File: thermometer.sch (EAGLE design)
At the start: 36 parts, among them IC1 MAX232, Q2 4 MHz, T1 BC547, T2 BC547, T3 BC547, T6 BC547, T7 BC547, T8 BC547, T9 BC547, X2 MINI-USB_SHIELD4P-85-32004-10X

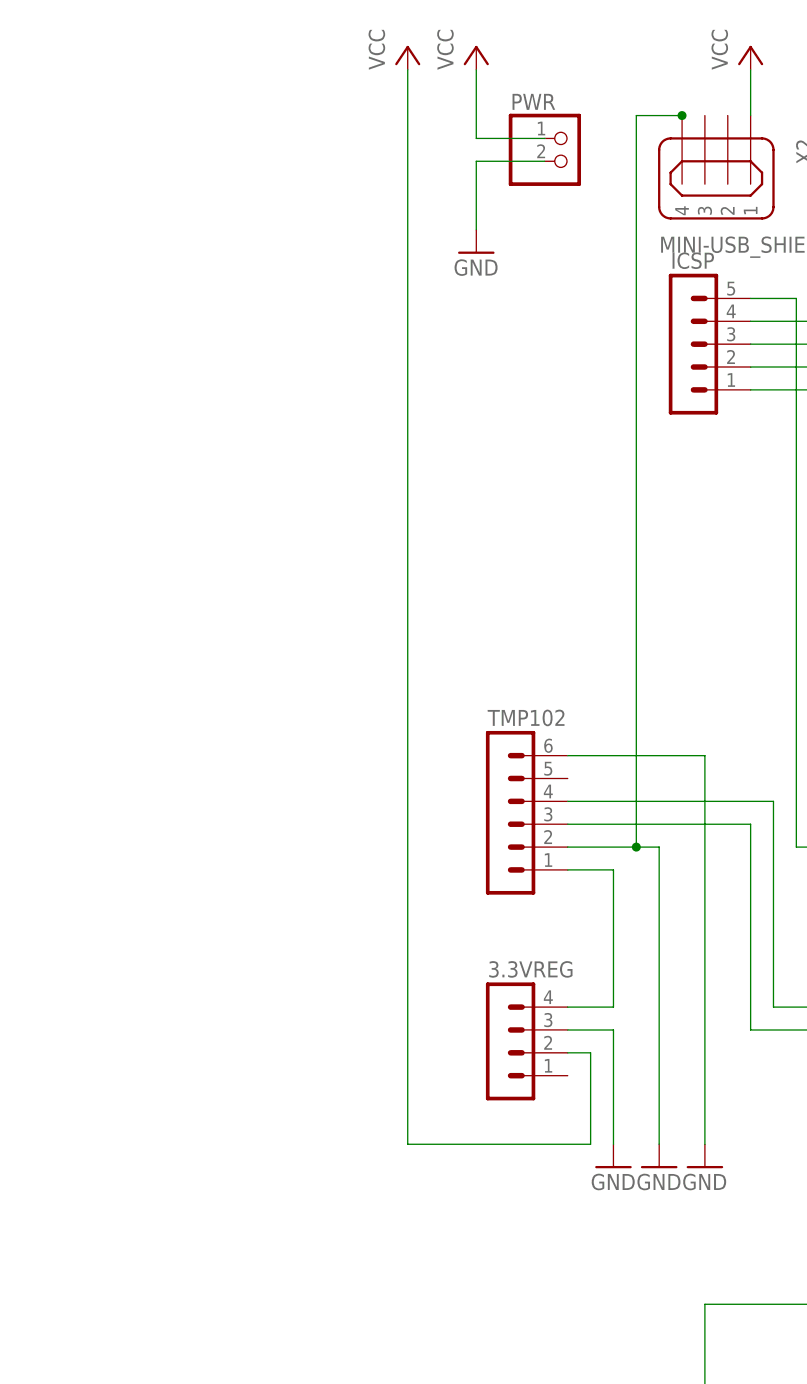
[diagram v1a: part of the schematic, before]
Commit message: Adding schematic and board as images
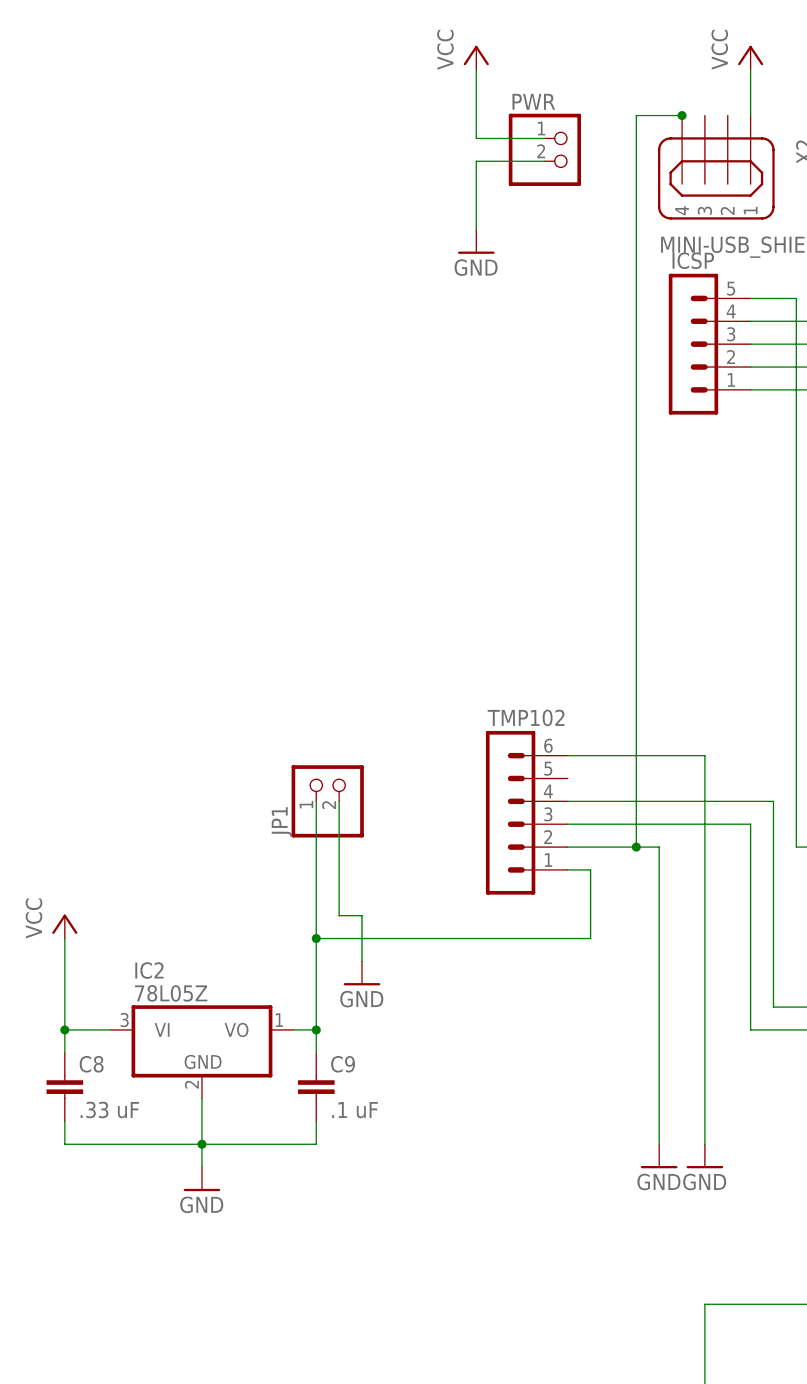
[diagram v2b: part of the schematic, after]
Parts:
- removed 3.3VREG: (no value), con-lstb:MA04-1
- added C8: .33 uF, rcl:C-EU050-025X075
- added C9: .1 uF, rcl:C-EU050-025X075
- added IC2: 78L05Z, linear:78L05Z
- added JP1: (no value), pinhead:PINHD-1X2
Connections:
- removed net N$32: 3.3VREG.4, TMP102.1
- new net N$48: C9.1, IC2.VO, JP1.1, TMP102.1
- net GND: now also C8.2, C9.2, IC2.GND, JP1.2; no longer 3.3VREG.3
- net VCC: now also C8.1, IC2.VI; no longer 3.3VREG.2
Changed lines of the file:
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@@
 <part name="ICSP" library="con-lstb" deviceset="MA05-1" device=""/>
 <part name="TMP102" library="con-lstb" deviceset="MA06-1" device=""/>
-<part name="3.3VREG" library="con-lstb" deviceset="MA04-1" device=""/>
-<part name="P+5" library="supply1" deviceset="VCC" device=""/>
-<part name="GND14" library="supply1" deviceset="GND" device=""/>
 <part name="GND15" library="supply1" deviceset="GND" device=""/>
 <part name="GND16" library="supply1" deviceset="GND" device=""/>
@@
 <part name="X2" library="con-cypressindustries" deviceset="MINI-USB_SHIELD4P-" device="85-32004-10X"/>
 <part name="P+8" library="supply1" deviceset="VCC" device=""/>
+<part name="IC2" library="linear" deviceset="78*" device="Z" technology="L05"/>
+<part name="C8" library="rcl" deviceset="C-EU" device="050-025X075" value=".33 uF"/>
+<part name="C9" library="rcl" deviceset="C-EU" device="050-025X075" value=".1 uF"/>
+<part name="GND20" library="supply1" deviceset="GND" device=""/>
+<part name="P+9" library="supply1" deviceset="VCC" device=""/>
+<part name="JP1" library="pinhead" deviceset="PINHD-1X2" device=""/>
+<part name="GND21" library="supply1" deviceset="GND" device=""/>
 </parts>
 <sheets>
@@
 <instance part="ICSP" gate="G$1" x="-55.88" y="210.82"/>
 <instance part="TMP102" gate="1" x="-76.2" y="160.02"/>
-<instance part="3.3VREG" gate="1" x="-76.2" y="134.62"/>
-<instance part="P+5" gate="VCC" x="-86.36" y="243.84"/>
-<instance part="GND14" gate="1" x="-63.5" y="119.38"/>
 <instance part="GND15" gate="1" x="-58.42" y="119.38"/>
 <instance part="GND16" gate="1" x="-53.34" y="119.38"/>
@@
 <instance part="X2" gate="G$1" x="-53.34" y="231.14" rot="R270"/>
 <instance part="P+8" gate="VCC" x="-48.26" y="243.84"/>
+<instance part="IC2" gate="A1" x="-109.22" y="134.62"/>
+<instance part="C8" gate="G$1" x="-124.46" y="129.54"/>
+<instance part="C9" gate="G$1" x="-96.52" y="129.54"/>
+<instance part="GND20" gate="1" x="-109.22" y="116.84"/>
+<instance part="P+9" gate="VCC" x="-124.46" y="147.32"/>
+<instance part="JP1" gate="G$1" x="-93.98" y="162.56" rot="R90"/>
+<instance part="GND21" gate="1" x="-91.44" y="139.7"/>
 </instances>
 <busses>
@@
 <wire x1="-48.26" y1="210.82" x2="-35.56" y2="210.82" width="0.1524" layer="91"/>
 <wire x1="-35.56" y1="210.82" x2="-35.56" y2="185.42" width="0.1524" layer="91"/>
-</segment>
-<segment>
-<pinref part="3.3VREG" gate="1" pin="3"/>
-<pinref part="GND14" gate="1" pin="GND"/>
-<wire x1="-68.58" y1="134.62" x2="-63.5" y2="134.62" width="0.1524" layer="91"/>
-<wire x1="-63.5" y1="134.62" x2="-63.5" y2="121.92" width="0.1524" layer="91"/>
 </segment>
 <segment>
@@
 <wire x1="-71.12" y1="231.14" x2="-78.74" y2="231.14" width="0.1524" layer="91"/>
 <wire x1="-78.74" y1="231.14" x2="-78.74" y2="223.52" width="0.1524" layer="91"/>
+</segment>
+<segment>
+<pinref part="IC2" gate="A1" pin="GND"/>
+<pinref part="GND20" gate="1" pin="GND"/>
+<wire x1="-109.22" y1="127" x2="-109.22" y2="121.92" width="0.1524" layer="91"/>
+<pinref part="C8" gate="G$1" pin="2"/>
+<wire x1="-109.22" y1="121.92" x2="-109.22" y2="119.38" width="0.1524" layer="91"/>
+<wire x1="-124.46" y1="124.46" x2="-124.46" y2="121.92" width="0.1524" layer="91"/>
+<wire x1="-124.46" y1="121.92" x2="-109.22" y2="121.92" width="0.1524" layer="91"/>
+<pinref part="C9" gate="G$1" pin="2"/>
+<wire x1="-96.52" y1="124.46" x2="-96.52" y2="121.92" width="0.1524" layer="91"/>
+<wire x1="-96.52" y1="121.92" x2="-109.22" y2="121.92" width="0.1524" layer="91"/>
+<junction x="-109.22" y="121.92"/>
+</segment>
+<segment>
+<pinref part="JP1" gate="G$1" pin="2"/>
+<wire x1="-93.98" y1="160.02" x2="-93.98" y2="147.32" width="0.1524" layer="91"/>
+<pinref part="GND21" gate="1" pin="GND"/>
+<wire x1="-93.98" y1="147.32" x2="-91.44" y2="147.32" width="0.1524" layer="91"/>
+<wire x1="-91.44" y1="147.32" x2="-91.44" y2="142.24" width="0.1524" layer="91"/>
 </segment>
 </net>
@@
 </segment>
 <segment>
-<pinref part="P+5" gate="VCC" pin="VCC"/>
-<wire x1="-86.36" y1="241.3" x2="-86.36" y2="121.92" width="0.1524" layer="91"/>
-<wire x1="-86.36" y1="121.92" x2="-66.04" y2="121.92" width="0.1524" layer="91"/>
-<wire x1="-66.04" y1="121.92" x2="-66.04" y2="132.08" width="0.1524" layer="91"/>
-<pinref part="3.3VREG" gate="1" pin="2"/>
-<wire x1="-66.04" y1="132.08" x2="-68.58" y2="132.08" width="0.1524" layer="91"/>
-</segment>
-<segment>
 <pinref part="C6" gate="G$1" pin="-"/>
 <pinref part="P+6" gate="VCC" pin="VCC"/>
@@
 <pinref part="X2" gate="G$1" pin="1"/>
 <wire x1="-48.26" y1="241.3" x2="-48.26" y2="236.22" width="0.1524" layer="91"/>
+</segment>
+<segment>
+<pinref part="IC2" gate="A1" pin="VI"/>
+<pinref part="C8" gate="G$1" pin="1"/>
+<wire x1="-119.38" y1="134.62" x2="-124.46" y2="134.62" width="0.1524" layer="91"/>
+<wire x1="-124.46" y1="134.62" x2="-124.46" y2="132.08" width="0.1524" layer="91"/>
+<pinref part="P+9" gate="VCC" pin="VCC"/>
+<wire x1="-124.46" y1="144.78" x2="-124.46" y2="134.62" width="0.1524" layer="91"/>
+<junction x="-124.46" y="134.62"/>
 </segment>
 </net>
@@
 <pinref part="PIC16F877A" gate="A" pin="RB7/PGD"/>
 <wire x1="-40.64" y1="157.48" x2="30.48" y2="157.48" width="0.1524" layer="91"/>
-</segment>
-</net>
-<net name="N$32" class="0">
-<segment>
-<pinref part="TMP102" gate="1" pin="1"/>
-<wire x1="-68.58" y1="152.4" x2="-63.5" y2="152.4" width="0.1524" layer="91"/>
-<wire x1="-63.5" y1="152.4" x2="-63.5" y2="137.16" width="0.1524" layer="91"/>
-<pinref part="3.3VREG" gate="1" pin="4"/>
-<wire x1="-63.5" y1="137.16" x2="-68.58" y2="137.16" width="0.1524" layer="91"/>
 </segment>
 </net>
@@
 </segment>
 </net>
+<net name="N$48" class="0">
+<segment>
+<pinref part="IC2" gate="A1" pin="VO"/>
+<pinref part="C9" gate="G$1" pin="1"/>
+<wire x1="-99.06" y1="134.62" x2="-96.52" y2="134.62" width="0.1524" layer="91"/>
+<wire x1="-96.52" y1="134.62" x2="-96.52" y2="132.08" width="0.1524" layer="91"/>
+<pinref part="JP1" gate="G$1" pin="1"/>
+<wire x1="-96.52" y1="134.62" x2="-96.52" y2="144.78" width="0.1524" layer="91"/>
+<junction x="-96.52" y="134.62"/>
+<pinref part="TMP102" gate="1" pin="1"/>
+<wire x1="-96.52" y1="144.78" x2="-96.52" y2="160.02" width="0.1524" layer="91"/>
+<wire x1="-68.58" y1="152.4" x2="-66.04" y2="152.4" width="0.1524" layer="91"/>
+<wire x1="-66.04" y1="152.4" x2="-66.04" y2="144.78" width="0.1524" layer="91"/>
+<wire x1="-66.04" y1="144.78" x2="-96.52" y2="144.78" width="0.1524" layer="91"/>
+<junction x="-96.52" y="144.78"/>
+</segment>
+</net>

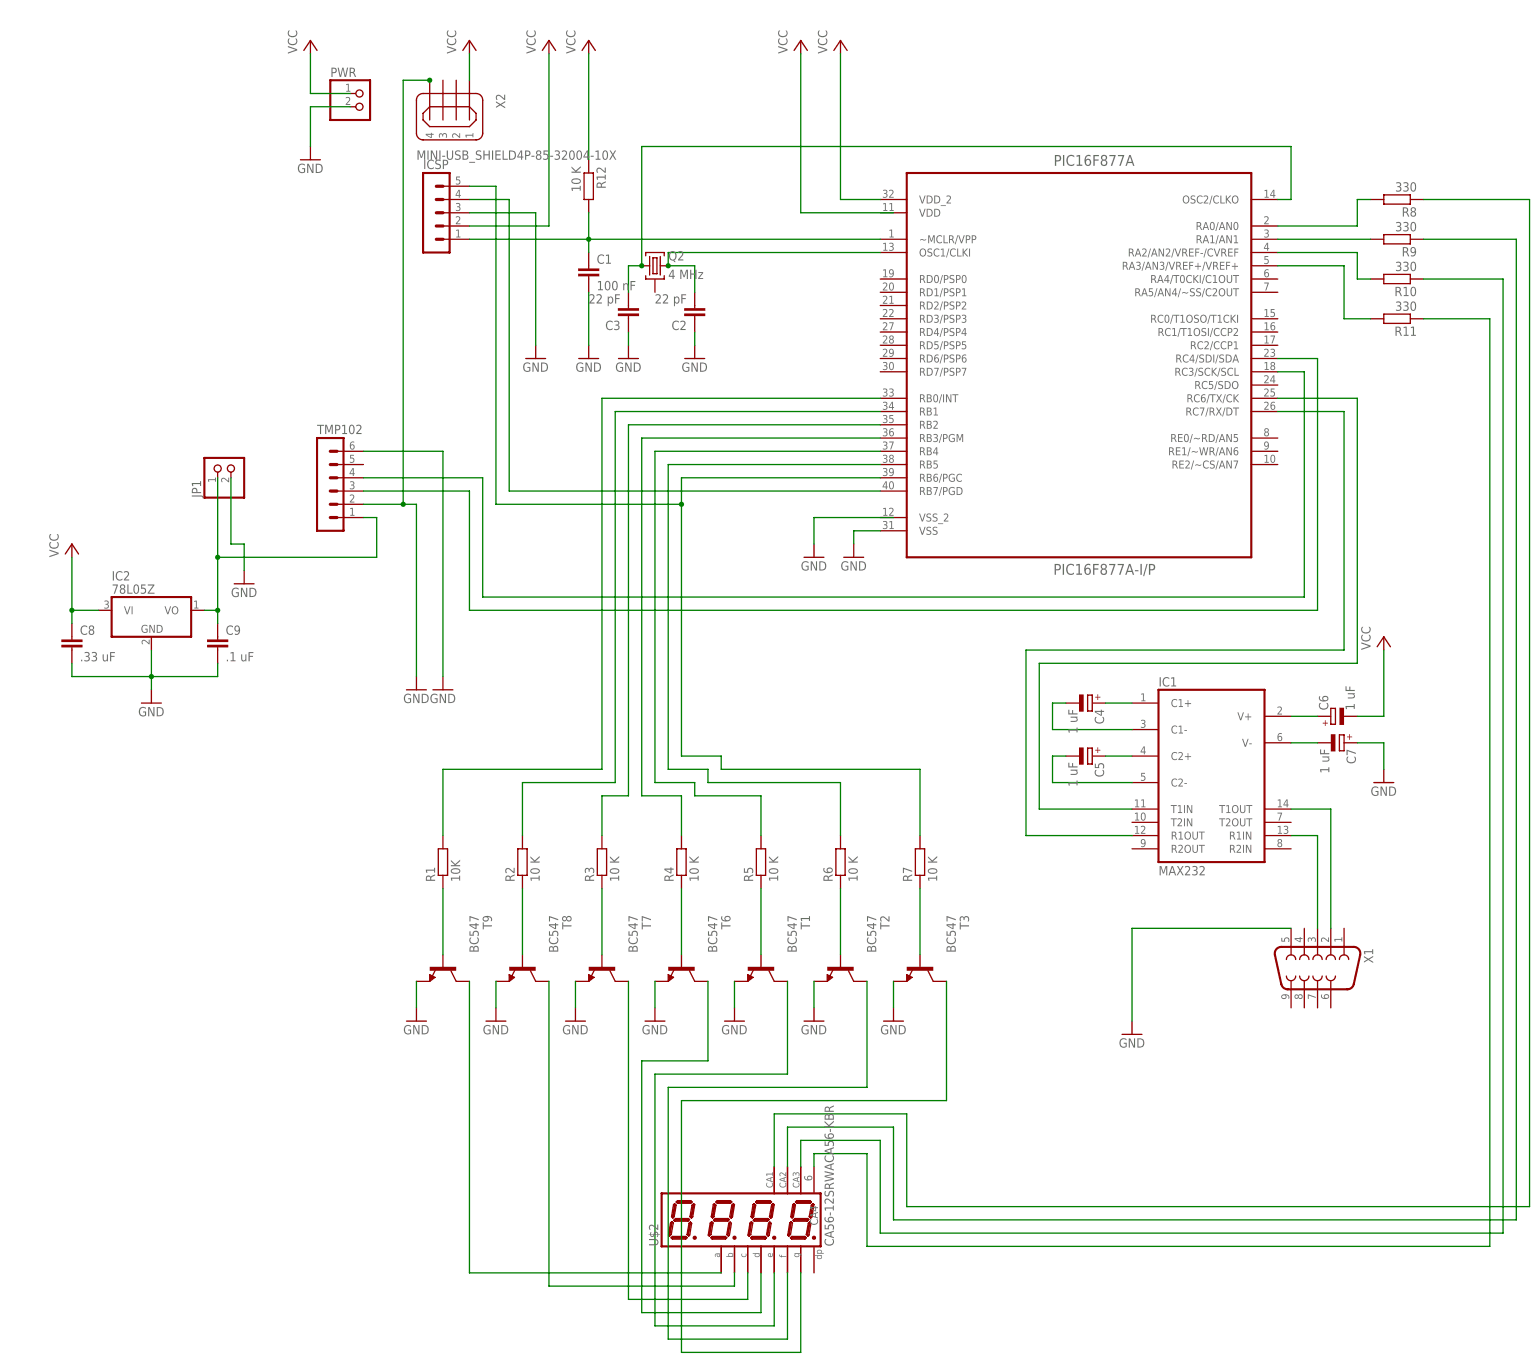
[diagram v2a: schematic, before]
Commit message: Version 2.0 with TCN75 and USB Micro B
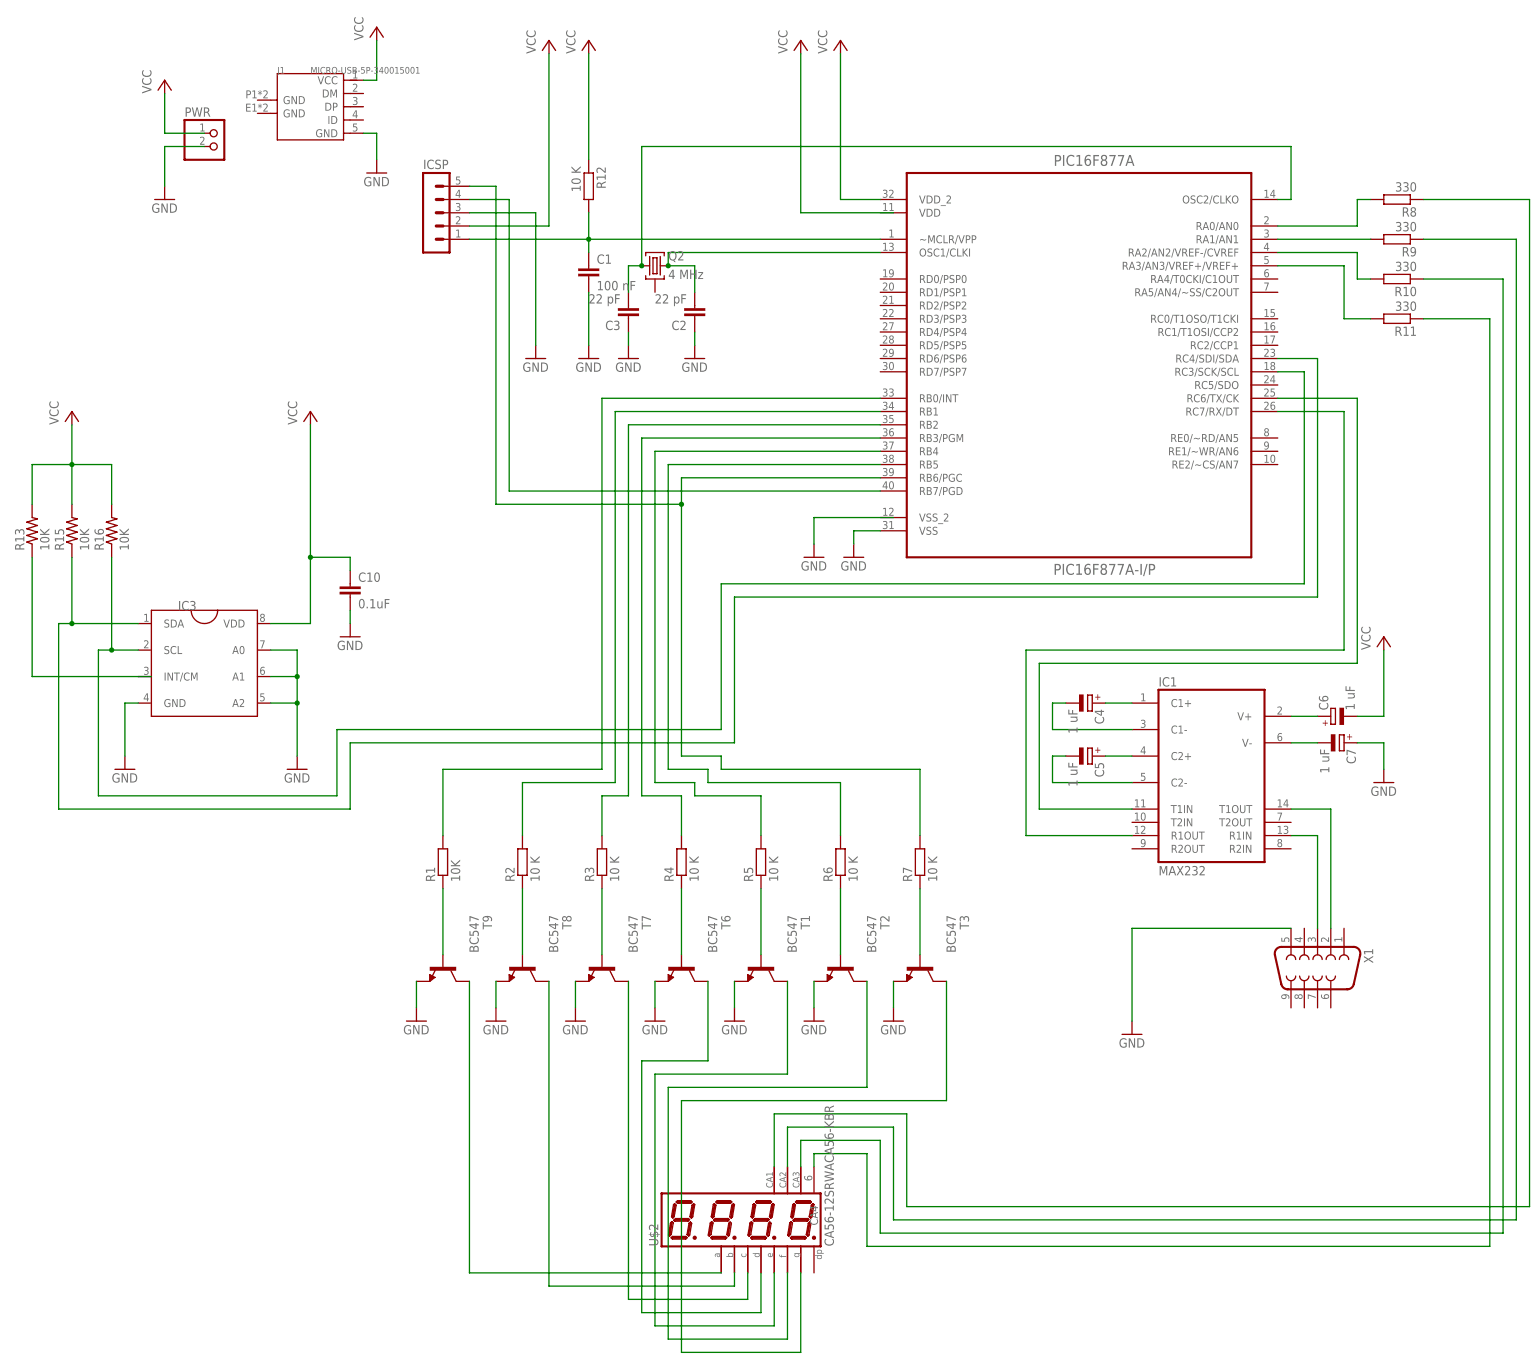
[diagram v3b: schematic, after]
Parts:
- removed C8: .33 uF, rcl:C-EU050-025X075
- removed C9: .1 uF, rcl:C-EU050-025X075
- removed IC2: 78L05Z, linear:78L05Z
- removed JP1: (no value), pinhead:PINHD-1X2
- removed TMP102: (no value), con-lstb:MA06-1
- removed X2: MINI-USB_SHIELD4P-85-32004-10X, con-cypressindustries:MINI-USB_SHIELD4P-85-32004-10X
- added C10: 0.1uF, SparkFun-Capacitors:0.1UF-25V-5%(0603)
- added IC3: (no value), instruction_set:TCN75TCN75MUA
- added J1: MICRO-USB-5P-340015001, Connector:MICRO-USB-5P-340015001
- added R13, R15, R16: 10K, SparkFun-Resistors:10KOHM-1/10W-1%(0603)0603
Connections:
- removed net N$34: PIC16F877A.RC4/SDI/SDA, TMP102.3
- removed net N$48: C9.1, IC2.VO, JP1.1, TMP102.1
- new net N$32: IC3.SCL, PIC16F877A.RC3/SCK/SCL, R16.1
- new net N$49: IC3.INT/CM, R13.1
- net GND: now also C10.2, IC3.A0, IC3.A1, IC3.A2, IC3.GND, J1.GND@1; no longer C8.2, C9.2, IC2.GND, JP1.2, TMP102.2, TMP102.6, X2G$1.4
- net N$33: now also IC3.SDA, PIC16F877A.RC4/SDI/SDA, R15.1; no longer PIC16F877A.RC3/SCK/SCL, TMP102.4
- net VCC: now also C10.1, IC3.VDD, J1.VCC, R13.2, R15.2, R16.2; no longer C8.1, IC2.VI, X2G$1.1
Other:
- moved on the sheet: PWR
